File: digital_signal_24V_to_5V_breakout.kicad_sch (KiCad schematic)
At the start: 5 parts, among them J1 Conn_01x04_Male, J2 Conn_01x04_Female, U1 LM22676MR-ADJ{slash}NOPB

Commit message: wip new design
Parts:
- added H3, H4: MountingHole, MountingHole:MountingHole_2.7mm_M2.5, symbol Mechanical:MountingHole
- H1, H2: footprint MountingHole:MountingHole_3.2mm_M3 -> MountingHole:MountingHole_2.7mm_M2.5
- J1, J2: footprint Connector_Molex:Molex_Micro-Fit_3.0_43045-0400_2x02_P3.00mm_Horizontal -> project:Molex_Micro-Fit_3.0_43045-0412_2x02_P3.00mm_Vertical
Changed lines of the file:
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@@
     (pin "1")
+  )
+  (symbol (lib_id "Mechanical:MountingHole") (at 180.34 154.94 0) (unit 1)
+    (in_bom yes) (on_board yes) (fields_autoplaced)
+    (property "Reference" "H4" (id 0) (at 182.88 153.6699 0)
+      (effects (font (size 1.27 1.27)) (justify left))
+    )
+    (property "Value" "MountingHole" (id 1) (at 182.88 156.2099 0)
+      (effects (font (size 1.27 1.27)) (justify left))
+    )
+    (property "Footprint" "MountingHole:MountingHole_2.7mm_M2.5" (id 2) (at 180.34 154.94 0)
+      (effects (font (size 1.27 1.27)) hide)
+    )
+    (property "Datasheet" "~" (id 3) (at 180.34 154.94 0)
+      (effects (font (size 1.27 1.27)) hide)
+    )
   )
   (symbol (lib_id "power:+5V") (at 257.81 46.99 0) (unit 1)
@@
       (effects (font (size 1.27 1.27)) (justify left))
     )
-    (property "Footprint" "MountingHole:MountingHole_3.2mm_M3" (id 2) (at 180.34 136.525 0)
+    (property "Footprint" "MountingHole:MountingHole_2.7mm_M2.5" (id 2) (at 180.34 136.525 0)
       (effects (font (size 1.27 1.27)) hide)
     )
@@
       (effects (font (size 1.27 1.27)) (justify right))
     )
-    (property "Footprint" "Connector_Molex:Molex_Micro-Fit_3.0_43045-0400_2x02_P3.00mm_Horizontal" (id 2) (at 265.43 55.88 0)
+    (property "Footprint" "project:Molex_Micro-Fit_3.0_43045-0412_2x02_P3.00mm_Vertical" (id 2) (at 265.43 55.88 0)
       (effects (font (size 1.27 1.27)) hide)
     )
@@
       (effects (font (size 1.27 1.27)) (justify left))
     )
-    (property "Footprint" "MountingHole:MountingHole_3.2mm_M3" (id 2) (at 180.34 142.875 0)
+    (property "Footprint" "MountingHole:MountingHole_2.7mm_M2.5" (id 2) (at 180.34 142.875 0)
       (effects (font (size 1.27 1.27)) hide)
     )
@@
     (property "Reference" "J2" (id 0) (at 38.1 55.88 0))
     (property "Value" "Conn_01x04_Female" (id 1) (at 34.29 62.23 0))
-    (property "Footprint" "Connector_Molex:Molex_Micro-Fit_3.0_43045-0400_2x02_P3.00mm_Horizontal" (id 2) (at 40.64 55.88 0)
+    (property "Footprint" "project:Molex_Micro-Fit_3.0_43045-0412_2x02_P3.00mm_Vertical" (id 2) (at 40.64 55.88 0)
       (effects (font (size 1.27 1.27)) hide)
     )
@@
     )
     (pin "1")
+  )
+  (symbol (lib_id "Mechanical:MountingHole") (at 180.34 148.59 0) (unit 1)
+    (in_bom yes) (on_board yes) (fields_autoplaced)
+    (property "Reference" "H3" (id 0) (at 182.88 147.3199 0)
+      (effects (font (size 1.27 1.27)) (justify left))
+    )
+    (property "Value" "MountingHole" (id 1) (at 182.88 149.8599 0)
+      (effects (font (size 1.27 1.27)) (justify left))
+    )
+    (property "Footprint" "MountingHole:MountingHole_2.7mm_M2.5" (id 2) (at 180.34 148.59 0)
+      (effects (font (size 1.27 1.27)) hide)
+    )
+    (property "Datasheet" "~" (id 3) (at 180.34 148.59 0)
+      (effects (font (size 1.27 1.27)) hide)
+    )
   )
   (symbol (lib_id "LM22676MR-ADJ_NOPB:LM22676MR-ADJ{brace}slash}NOPB") (at 104.775 144.78 0) (unit 1)
@@
     )
     (path "/3ddefe5d-76a3-4b3e-9cf5-520634f2cdc1"
-      (reference "H1") (unit 1) (value "MountingHole") (footprint "MountingHole:MountingHole_3.2mm_M3")
+      (reference "H1") (unit 1) (value "MountingHole") (footprint "MountingHole:MountingHole_2.7mm_M2.5")
     )
     (path "/6c12e3bc-cf0b-44ce-b562-b88ad2c665a7"
-      (reference "H2") (unit 1) (value "MountingHole") (footprint "MountingHole:MountingHole_3.2mm_M3")
+      (reference "H2") (unit 1) (value "MountingHole") (footprint "MountingHole:MountingHole_2.7mm_M2.5")
+    )
+    (path "/ddc98683-f476-4ab7-a72d-ce80280d4d00"
+      (reference "H3") (unit 1) (value "MountingHole") (footprint "MountingHole:MountingHole_2.7mm_M2.5")
+    )
+    (path "/10481a5b-9485-49c1-b9b2-41789d7310e6"
+      (reference "H4") (unit 1) (value "MountingHole") (footprint "MountingHole:MountingHole_2.7mm_M2.5")
     )
     (path "/698dd092-e5c3-4b8b-b20b-1422a03bec2d"
-      (reference "J1") (unit 1) (value "Conn_01x04_Male") (footprint "Connector_Molex:Molex_Micro-Fit_3.0_43045-0400_2x02_P3.00mm_Horizontal")
+      (reference "J1") (unit 1) (value "Conn_01x04_Male") (footprint "project:Molex_Micro-Fit_3.0_43045-0412_2x02_P3.00mm_Vertical")
     )
     (path "/ba308514-61e0-409a-a199-b669f349e83b"
-      (reference "J2") (unit 1) (value "Conn_01x04_Female") (footprint "Connector_Molex:Molex_Micro-Fit_3.0_43045-0400_2x02_P3.00mm_Horizontal")
+      (reference "J2") (unit 1) (value "Conn_01x04_Female") (footprint "project:Molex_Micro-Fit_3.0_43045-0412_2x02_P3.00mm_Vertical")
     )
     (path "/7b1e1b5c-3e4b-4b50-80bd-6f7cf89a03de/cf529915-5499-41d3-9110-9622db8c7486"

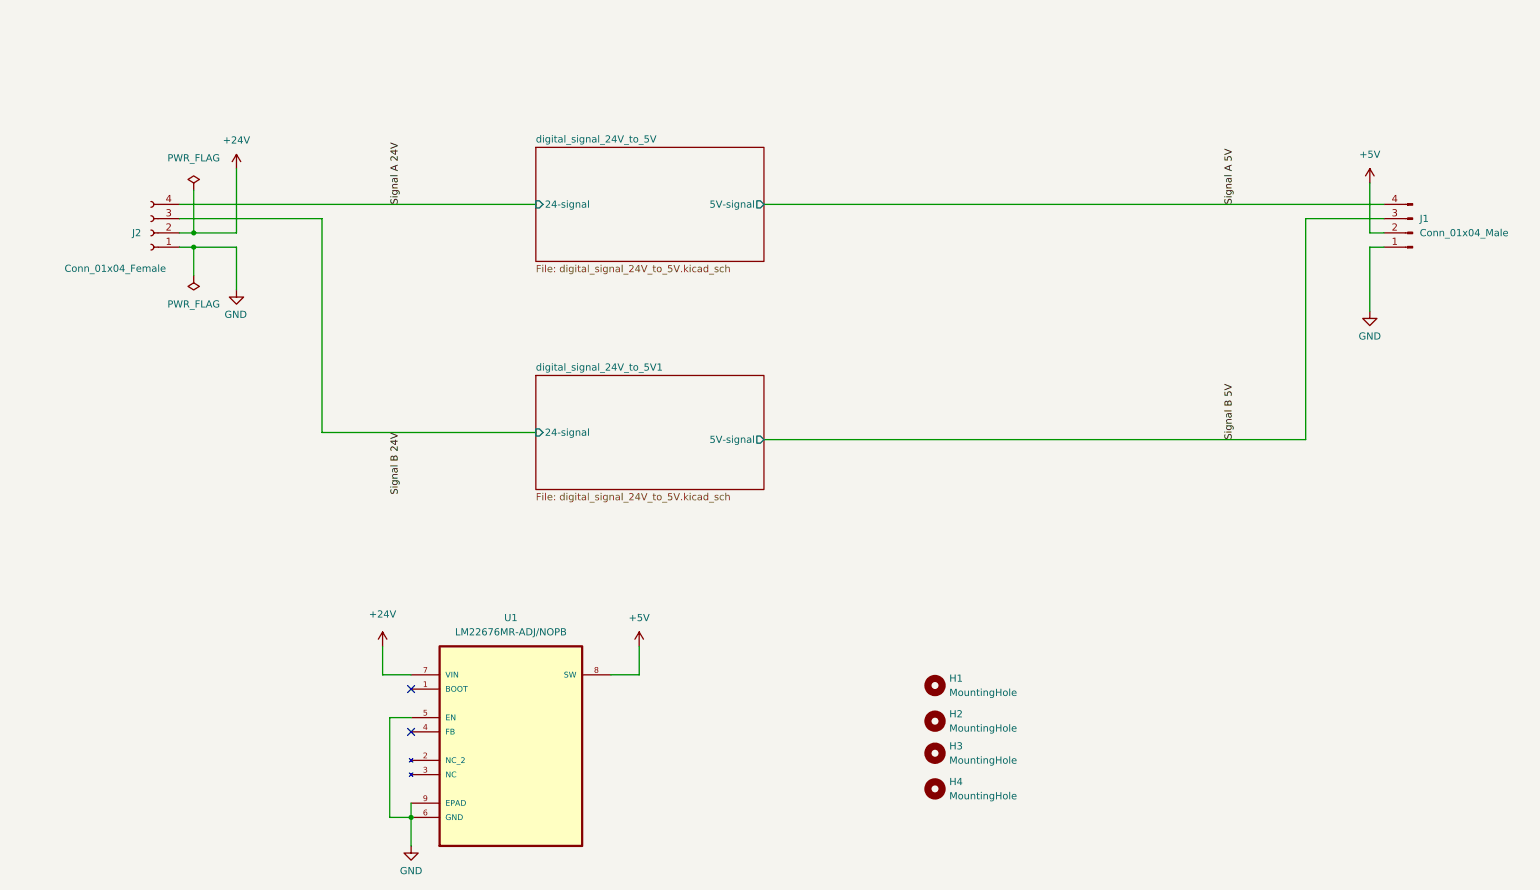
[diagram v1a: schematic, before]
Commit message: 4x opto couplers
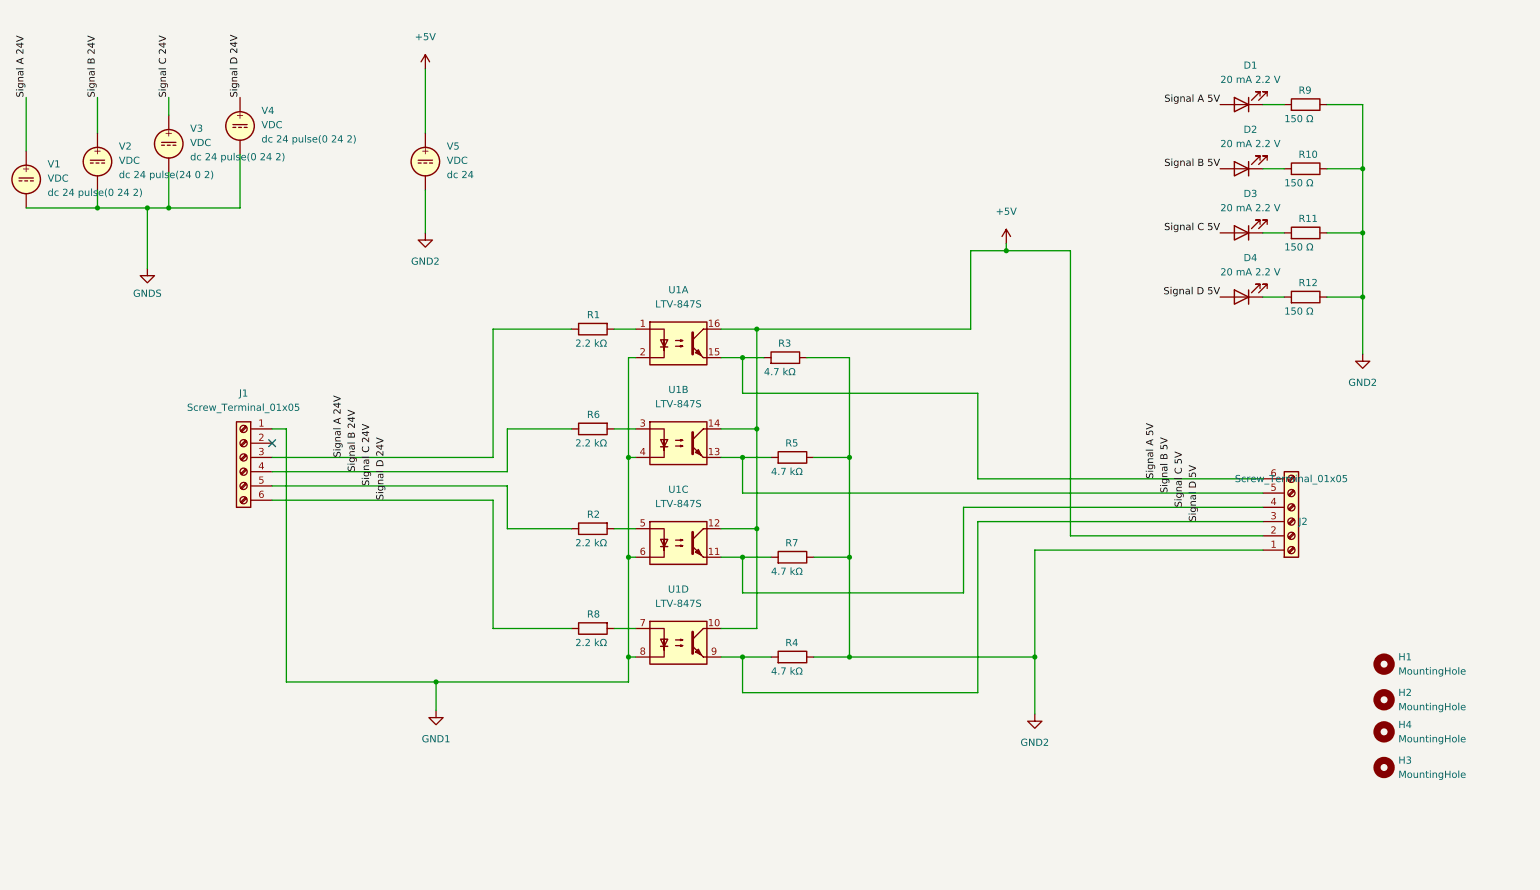
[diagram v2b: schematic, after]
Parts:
- removed J1: Conn_01x04_Male, project:Molex_Micro-Fit_3.0_43045-0412_2x02_P3.00mm_Vertical, symbol Connector:Conn_01x04_Male
- removed J2: Conn_01x04_Female, project:Molex_Micro-Fit_3.0_43045-0412_2x02_P3.00mm_Vertical, symbol Connector:Conn_01x04_Female
- removed U1: LM22676MR-ADJ/NOPB, Package_SO:Texas_HSOP-8-1EP_3.9x4.9mm_P1.27mm_ThermalVias, symbol LM22676MR-ADJ_NOPB:LM22676MR-ADJ{brace}slash}NOPB
- added D1, D2, D3, D4: 20 mA 2.2 V, LED_SMD:LED_0805_2012Metric, symbol Device:LED
- added J1, J2: Screw_Terminal_01x05, TerminalBlock_Phoenix:TerminalBlock_Phoenix_MKDS-3-6-5.08_1x06_P5.08mm_Horizontal, symbol Connector:Screw_Terminal_01x06
- added R1, R2, R6, R8: 2.2 kΩ, Resistor_SMD:R_0805_2012Metric, symbol Device:R
- added R10, R11, R12, R9: 150 Ω, Resistor_SMD:R_0805_2012Metric, symbol Device:R
- added R3, R4, R5, R7: 4.7 kΩ, Resistor_SMD:R_0805_2012Metric, symbol Device:R
- added U1: LTV-847S, Package_DIP:SMDIP-16_W9.53mm, symbol Isolator:LTV-847S
- added V1, V2, V3, V4, V5: VDC, symbol Simulation_SPICE:VDC
- renumbered H4 to H3, H3 to H4
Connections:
- net +5V: now also J2.2 (Pin_2), U1.10, U1.12, U1.14, U1.16, V5.1
- net Signal A 24V: now also J1.3 (Pin_3), R1.1, V1.1
- net Signal A 5V: now also D1.2 (A), J2.6 (Pin_6), R3.2, U1.15
- net Signal B 24V: now also J1.4 (Pin_4), R6.1, V2.1
- net Signal B 5V: now also D2.2 (A), J2.5 (Pin_5), R5.2, U1.13
- new net: R1.2, U1.1
- new net: R6.2, U1.3
- new net: D3.1 (K), R11.2
- new net: R2.2, U1.5
- new net: D2.1 (K), R10.2
- new net: D1.1 (K), R9.2
- new net: D4.1 (K), R12.2
- new net: R8.2, U1.7
- new net GND1: J1.1 (Pin_1), U1.2, U1.4, U1.6, U1.8
- new net GND2: J2.1 (Pin_1), R10.1, R11.1, R12.1, R3.1, R4.1, R5.1, R7.1, R9.1, V5.2
- new net GNDS: V1.2, V2.2, V3.2, V4.2
- new net Signal C 24V: J1.5 (Pin_5), R2.1, V3.1
- new net Signal C 5V: D3.2 (A), J2.4 (Pin_4), R7.2, U1.11
- new net Signal D 24V: J1.6 (Pin_6), R8.1, V4.1
- new net Signal D 5V: D4.2 (A), J2.3 (Pin_3), R4.2, U1.9
- no-connect marks 2 -> 1
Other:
- removed sheet digital_signal_24V_to_5V
- removed sheet digital_signal_24V_to_5V1
- moved on the sheet: H1, H2, H3, H4

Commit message: missed save, this is version sent to jlcpcb
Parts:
- J1, J2: footprint TerminalBlock_Phoenix:TerminalBlock_Phoenix_MKDS-3-6-5.08_1x06_P5.08mm_Horizontal -> Connector_Phoenix_MSTB:PhoenixContact_MSTBVA_2,5_6-G-5,08_1x06_P5.08mm_Vertical; MPN1 Phoenix Contacts:1701144 -> Phoenix Contacts:1755778; SKU1 Mouser:651-1701144 -> Mouser:651-1755778
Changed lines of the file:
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@@
     (property "Reference" "J1" (id 0) (at 57.15 84.455 0))
     (property "Value" "Screw_Terminal_01x05" (id 1) (at 57.15 86.995 0))
-    (property "Footprint" "TerminalBlock_Phoenix:TerminalBlock_Phoenix_MKDS-3-6-5.08_1x06_P5.08mm_Horizontal" (id 2) (at 57.15 95.885 0)
+    (property "Footprint" "Connector_Phoenix_MSTB:PhoenixContact_MSTBVA_2,5_6-G-5,08_1x06_P5.08mm_Vertical" (id 2) (at 57.15 95.885 0)
       (effects (font (size 1.27 1.27)) hide)
     )
@@
       (effects (font (size 1.27 1.27)) hide)
     )
-    (property "MPN1" "Phoenix Contacts:1701144" (id 4) (at 57.15 95.885 0)
-      (effects (font (size 1.27 1.27)) hide)
-    )
-    (property "SKU1" "Mouser:651-1701144" (id 5) (at 57.15 95.885 0)
+    (property "MPN1" "Phoenix Contacts:1755778" (id 4) (at 57.15 95.885 0)
+      (effects (font (size 1.27 1.27)) hide)
+    )
+    (property "SKU1" "Mouser:651-1755778" (id 5) (at 57.15 95.885 0)
       (effects (font (size 1.27 1.27)) hide)
     )
@@
     )
     (property "Value" "Screw_Terminal_01x05" (id 1) (at 243.84 99.695 0))
-    (property "Footprint" "TerminalBlock_Phoenix:TerminalBlock_Phoenix_MKDS-3-6-5.08_1x06_P5.08mm_Horizontal" (id 2) (at 243.84 107.315 0)
+    (property "Footprint" "Connector_Phoenix_MSTB:PhoenixContact_MSTBVA_2,5_6-G-5,08_1x06_P5.08mm_Vertical" (id 2) (at 243.84 107.315 0)
       (effects (font (size 1.27 1.27)) hide)
     )
@@
       (effects (font (size 1.27 1.27)) hide)
     )
-    (property "MPN1" "Phoenix Contacts:1701144" (id 4) (at 243.84 107.315 0)
-      (effects (font (size 1.27 1.27)) hide)
-    )
-    (property "SKU1" "Mouser:651-1701144" (id 5) (at 243.84 107.315 0)
+    (property "MPN1" "Phoenix Contacts:1755778" (id 4) (at 243.84 107.315 0)
+      (effects (font (size 1.27 1.27)) hide)
+    )
+    (property "SKU1" "Mouser:651-1755778" (id 5) (at 243.84 107.315 0)
       (effects (font (size 1.27 1.27)) hide)
     )
@@
     )
     (path "/31f2d50b-cf26-4856-8413-7a5a522335c4"
-      (reference "J1") (unit 1) (value "Screw_Terminal_01x05") (footprint "TerminalBlock_Phoenix:TerminalBlock_Phoenix_MKDS-3-6-5.08_1x06_P5.08mm_Horizontal")
+      (reference "J1") (unit 1) (value "Screw_Terminal_01x05") (footprint "Connector_Phoenix_MSTB:PhoenixContact_MSTBVA_2,5_6-G-5,08_1x06_P5.08mm_Vertical")
     )
     (path "/6226a9b2-9c93-403b-8abe-9af1537bc3a8"
-      (reference "J2") (unit 1) (value "Screw_Terminal_01x05") (footprint "TerminalBlock_Phoenix:TerminalBlock_Phoenix_MKDS-3-6-5.08_1x06_P5.08mm_Horizontal")
+      (reference "J2") (unit 1) (value "Screw_Terminal_01x05") (footprint "Connector_Phoenix_MSTB:PhoenixContact_MSTBVA_2,5_6-G-5,08_1x06_P5.08mm_Vertical")
     )
     (path "/4ef75480-8d77-48cd-87b0-2421052a250c"

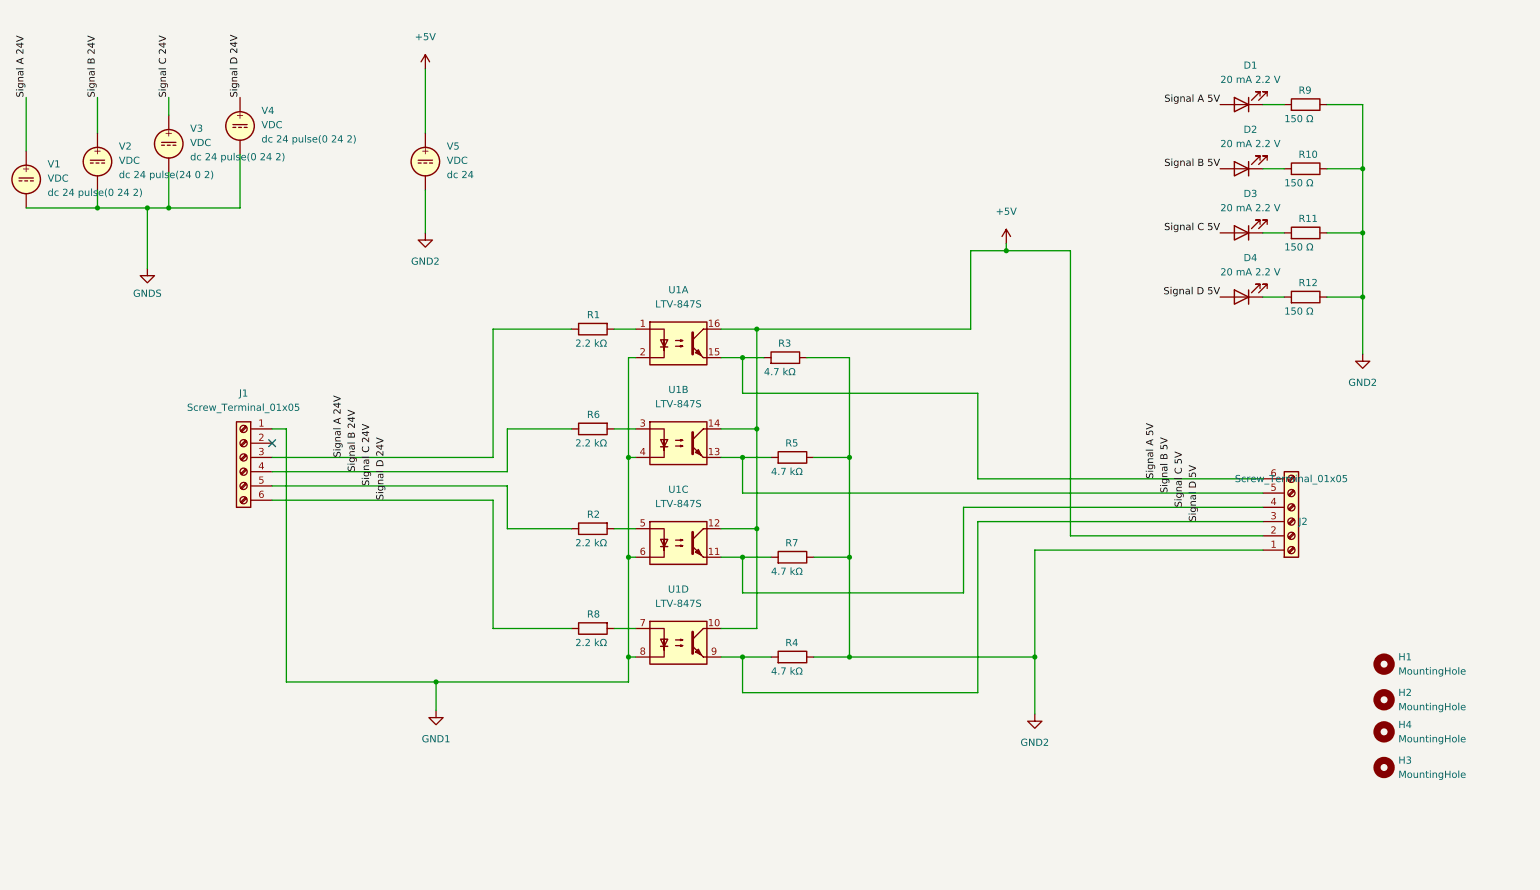
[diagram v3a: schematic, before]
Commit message: added hierachial pins for inclusion in fdm_3dp_setup
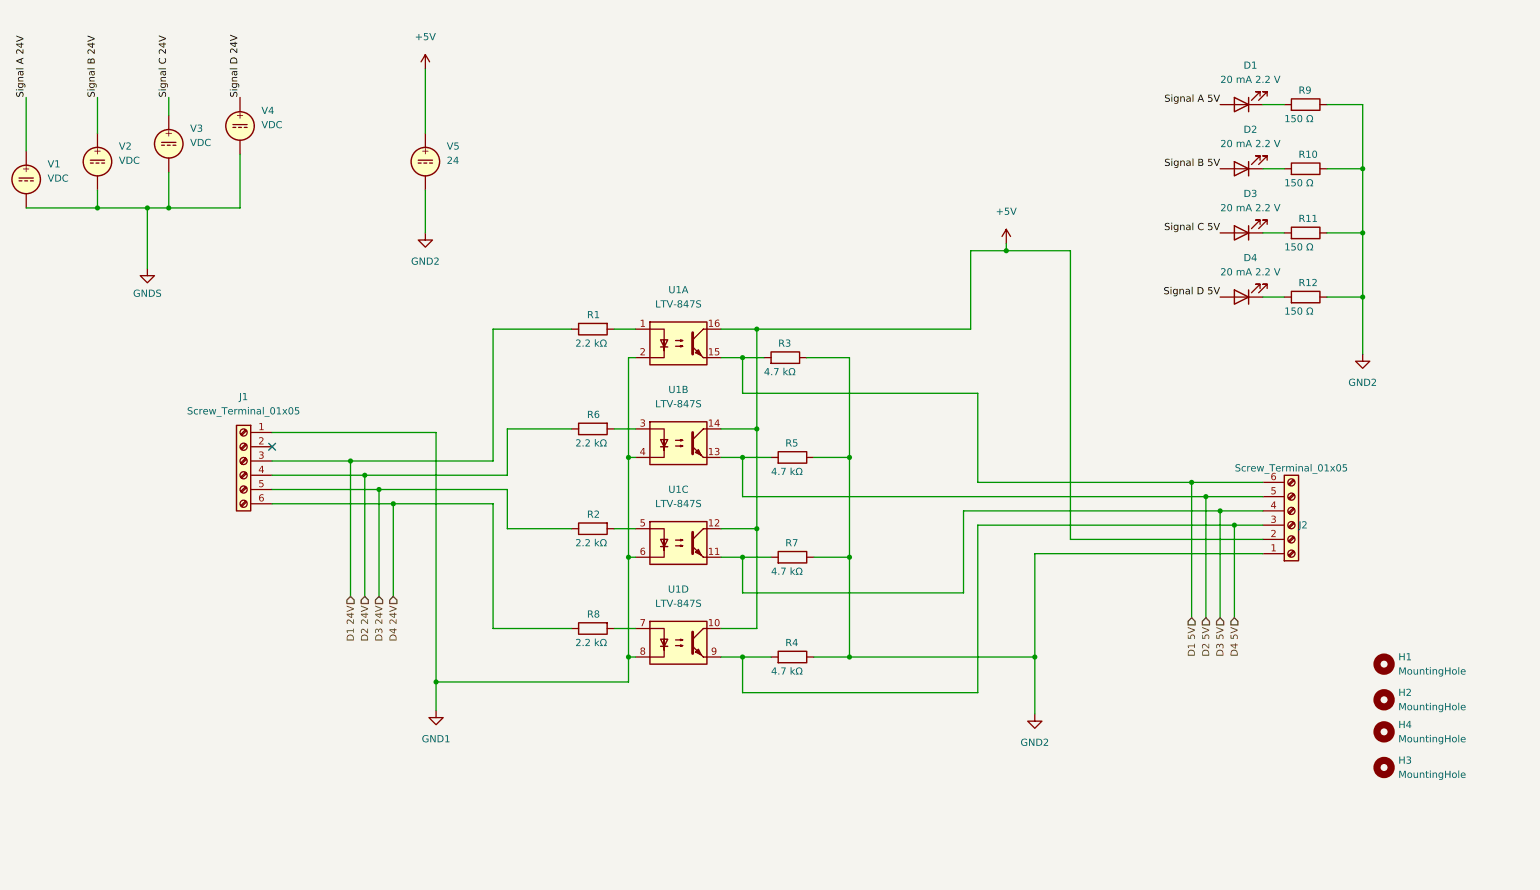
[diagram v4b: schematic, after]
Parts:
- V1, V3, V4: Spice_Model dc 24 pulse(0 24 2) -> (none); Spice_Netlist_Enabled Y -> (none); Spice_Primitive V -> (none)
- V2: Spice_Model dc 24 pulse(24 0 2) -> (none); Spice_Netlist_Enabled Y -> (none); Spice_Primitive V -> (none)
- V5: value VDC -> 24; Spice_Model dc 24 -> (none); Spice_Netlist_Enabled Y -> (none); Spice_Primitive V -> (none)
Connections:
- net Signal A 24V: no longer J1.3 (Pin_3), R1.1
- net Signal A 5V: no longer J2.6 (Pin_6), R3.2, U1.15
- net Signal B 24V: no longer J1.4 (Pin_4), R6.1
- net Signal B 5V: no longer J2.5 (Pin_5), R5.2, U1.13
- net Signal C 24V: no longer J1.5 (Pin_5), R2.1
- net Signal C 5V: no longer J2.4 (Pin_4), R7.2, U1.11
- net Signal D 24V: no longer J1.6 (Pin_6), R8.1
- net Signal D 5V: no longer J2.3 (Pin_3), R4.2, U1.9
- new net D1 24V: J1.3 (Pin_3), R1.1
- new net D1 5V: J2.6 (Pin_6), R3.2, U1.15
- new net D2 24V: J1.4 (Pin_4), R6.1
- new net D2 5V: J2.5 (Pin_5), R5.2, U1.13
- new net D3 24V: J1.5 (Pin_5), R2.1
- new net D3 5V: J2.4 (Pin_4), R7.2, U1.11
- new net D4 24V: J1.6 (Pin_6), R8.1
- new net D4 5V: J2.3 (Pin_3), R4.2, U1.9
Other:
- moved on the sheet: J1, J2
